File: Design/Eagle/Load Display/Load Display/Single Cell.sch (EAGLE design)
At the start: 1 part

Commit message: Added some eagle files
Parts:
- added 12VPOWER, 3.3VPOWER, I2C: M025MM, Ben-SF-Con:M025MM
- added R1, R2, R3, R4, R5, R6, R7: 200, Ben-rcl:R-US_0207/10
- added U$3: HT16K33BRD, Parts:HT16K33BRD
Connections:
- new net N$1: DIS1.A, R1.2
- new net N$10: R3.1, U$3.C2
- new net N$11: R4.1, U$3.C3
- new net N$12: R5.1, U$3.C4
- new net N$13: R6.1, U$3.C5
- new net N$14: R7.1, U$3.C6
- new net N$15: I2C.1, U$3.SDA
- new net N$16: I2C.2, U$3.SCL
- new net N$17: 12VPOWER.1, 3.3VPOWER.1, U$3.GND
- new net N$18: DIS1.DP, U$3.C7
- new net N$19: 3.3VPOWER.2, U$3.VDD
- new net N$2: DIS1.B, R2.2
- new net N$20: 12VPOWER.2, DIS1.CA, DIS1.CA@1
- new net N$3: DIS1.C, R3.2
- new net N$4: DIS1.D, R4.2
- new net N$5: DIS1.E, R5.2
- new net N$6: DIS1.F, R6.2
- new net N$7: DIS1.G, R7.2
- new net N$8: R1.1, U$3.C0
- new net N$9: R2.1, U$3.C1
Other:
- moved on the sheet: DIS1

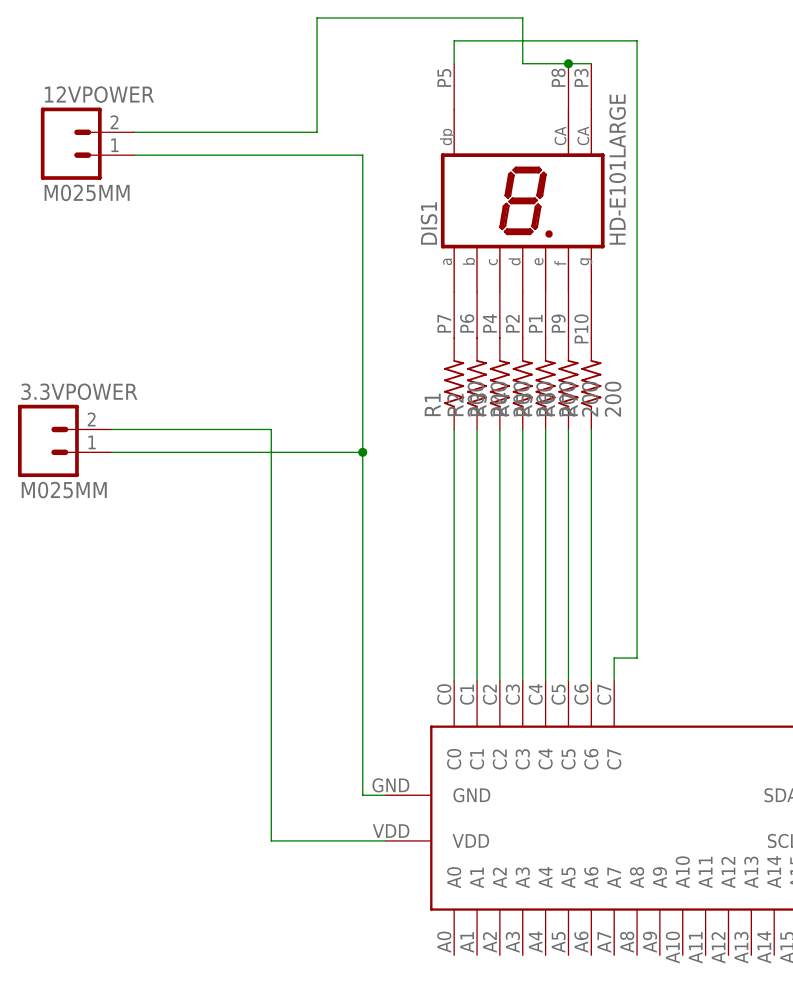
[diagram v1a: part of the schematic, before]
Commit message: Added a 5V regulator
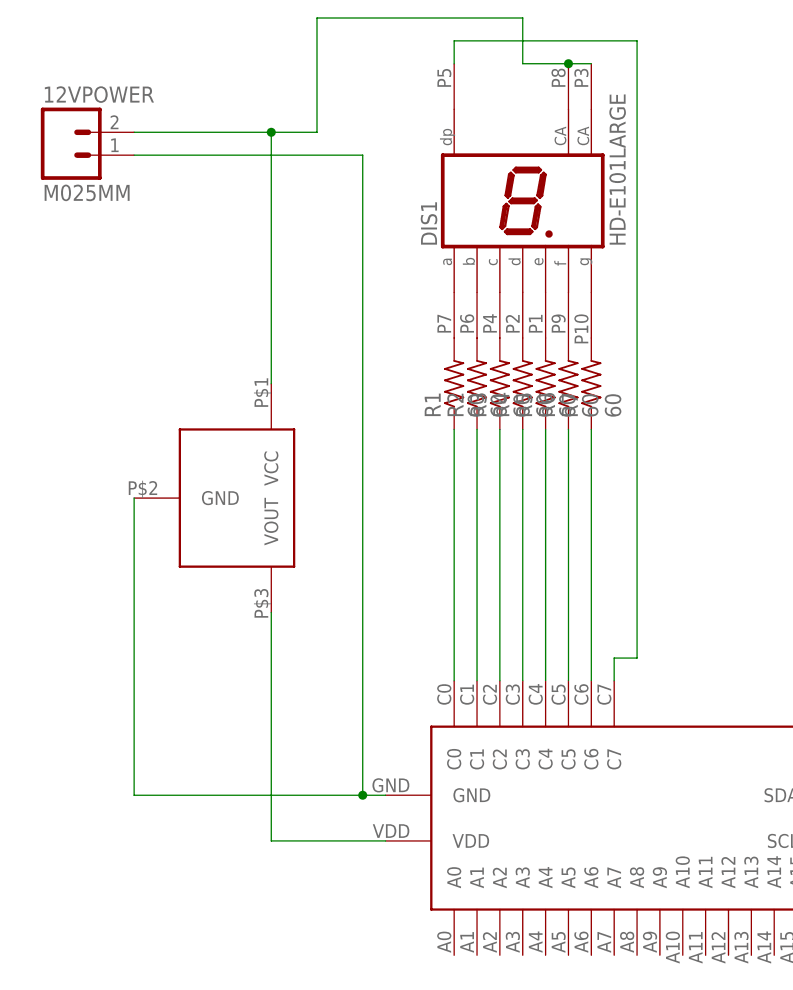
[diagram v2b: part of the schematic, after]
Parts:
- removed 3.3VPOWER: M025MM, Ben-SF-Con:M025MM
- added U$1: 5VREG, Parts:5VREG
- R1, R2, R3, R4, R5, R6, R7: value 200 -> 60
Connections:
- net N$17: now also U$1.GND; no longer 3.3VPOWER.1
- net N$19: now also U$1.VOUT; no longer 3.3VPOWER.2
- net N$20: now also U$1.VCC
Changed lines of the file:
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@@
 <part name="DIS1" library="Parts" deviceset="HD-E101" device="LARGE"/>
 <part name="U$3" library="Parts" deviceset="HT16K33BRD" device=""/>
-<part name="R1" library="Ben-rcl" deviceset="R-US_" device="0207/10" value="200"/>
-<part name="R2" library="Ben-rcl" deviceset="R-US_" device="0207/10" value="200"/>
-<part name="R3" library="Ben-rcl" deviceset="R-US_" device="0207/10" value="200"/>
-<part name="R4" library="Ben-rcl" deviceset="R-US_" device="0207/10" value="200"/>
-<part name="R5" library="Ben-rcl" deviceset="R-US_" device="0207/10" value="200"/>
-<part name="R6" library="Ben-rcl" deviceset="R-US_" device="0207/10" value="200"/>
-<part name="R7" library="Ben-rcl" deviceset="R-US_" device="0207/10" value="200"/>
+<part name="R1" library="Ben-rcl" deviceset="R-US_" device="0207/10" value="60"/>
+<part name="R2" library="Ben-rcl" deviceset="R-US_" device="0207/10" value="60"/>
+<part name="R3" library="Ben-rcl" deviceset="R-US_" device="0207/10" value="60"/>
+<part name="R4" library="Ben-rcl" deviceset="R-US_" device="0207/10" value="60"/>
+<part name="R5" library="Ben-rcl" deviceset="R-US_" device="0207/10" value="60"/>
+<part name="R6" library="Ben-rcl" deviceset="R-US_" device="0207/10" value="60"/>
+<part name="R7" library="Ben-rcl" deviceset="R-US_" device="0207/10" value="60"/>
 <part name="12VPOWER" library="Ben-SF-Con" deviceset="M02" device="5MM"/>
 <part name="I2C" library="Ben-SF-Con" deviceset="M02" device="5MM"/>
-<part name="3.3VPOWER" library="Ben-SF-Con" deviceset="M02" device="5MM"/>
+<part name="U$1" library="Parts" deviceset="5VREG" device=""/>
 </parts>
 <sheets>
@@
 <instance part="12VPOWER" gate="G$1" x="15.24" y="93.98"/>
 <instance part="I2C" gate="G$1" x="129.54" y="20.32" rot="R180"/>
-<instance part="3.3VPOWER" gate="G$1" x="12.7" y="60.96"/>
+<instance part="U$1" gate="G$1" x="38.1" y="55.88" rot="R270"/>
 </instances>
 <busses>
@@
 <pinref part="U$3" gate="G$1" pin="GND"/>
 <wire x1="50.8" y1="22.86" x2="48.26" y2="22.86" width="0.1524" layer="91"/>
-<wire x1="48.26" y1="22.86" x2="48.26" y2="60.96" width="0.1524" layer="91"/>
-<pinref part="3.3VPOWER" gate="G$1" pin="1"/>
-<wire x1="48.26" y1="60.96" x2="20.32" y2="60.96" width="0.1524" layer="91"/>
-<wire x1="48.26" y1="60.96" x2="48.26" y2="93.98" width="0.1524" layer="91"/>
-<junction x="48.26" y="60.96"/>
+<wire x1="48.26" y1="22.86" x2="48.26" y2="93.98" width="0.1524" layer="91"/>
 <pinref part="12VPOWER" gate="G$1" pin="1"/>
 <wire x1="48.26" y1="93.98" x2="22.86" y2="93.98" width="0.1524" layer="91"/>
+<pinref part="U$1" gate="G$1" pin="GND"/>
+<wire x1="48.26" y1="22.86" x2="22.86" y2="22.86" width="0.1524" layer="91"/>
+<wire x1="22.86" y1="22.86" x2="22.86" y2="55.88" width="0.1524" layer="91"/>
+<junction x="48.26" y="22.86"/>
 </segment>
 </net>
@@
 <pinref part="U$3" gate="G$1" pin="VDD"/>
 <wire x1="50.8" y1="17.78" x2="38.1" y2="17.78" width="0.1524" layer="91"/>
-<wire x1="38.1" y1="17.78" x2="38.1" y2="63.5" width="0.1524" layer="91"/>
-<pinref part="3.3VPOWER" gate="G$1" pin="2"/>
-<wire x1="38.1" y1="63.5" x2="20.32" y2="63.5" width="0.1524" layer="91"/>
+<pinref part="U$1" gate="G$1" pin="VOUT"/>
+<wire x1="38.1" y1="43.18" x2="38.1" y2="17.78" width="0.1524" layer="91"/>
 </segment>
 </net>
@@
 <wire x1="43.18" y1="109.22" x2="43.18" y2="96.52" width="0.1524" layer="91"/>
 <pinref part="12VPOWER" gate="G$1" pin="2"/>
-<wire x1="43.18" y1="96.52" x2="22.86" y2="96.52" width="0.1524" layer="91"/>
+<wire x1="43.18" y1="96.52" x2="38.1" y2="96.52" width="0.1524" layer="91"/>
+<pinref part="U$1" gate="G$1" pin="VCC"/>
+<wire x1="38.1" y1="96.52" x2="22.86" y2="96.52" width="0.1524" layer="91"/>
+<wire x1="38.1" y1="68.58" x2="38.1" y2="96.52" width="0.1524" layer="91"/>
+<junction x="38.1" y="96.52"/>
 </segment>
 </net>

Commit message: Added a lot of eagle stuff
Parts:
- DIS1: value HD-E101LARGE -> HD-E101BIG; device Parts:HD-E101LARGE -> Parts:HD-E101BIG
- R6, R7: device Ben-rcl:R-US_0207/10 -> Ben-rcl:R-US_0207/15
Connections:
- net N$20: no longer DIS1.CA
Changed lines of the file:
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@@
 <?xml version="1.0" encoding="utf-8"?>
 <!DOCTYPE eagle SYSTEM "eagle.dtd">
-<eagle version="6.2">
+<eagle version="6.5.0">
 <drawing>
 <settings>
@@
 <grid distance="0.1" unitdist="inch" unit="inch" style="lines" multiple="1" display="no" altdistance="0.01" altunitdist="inch" altunit="inch"/>
 <layers>
-<layer number="1" name="Top" color="4" fill="1" visible="no" active="no"/>
-<layer number="16" name="Bottom" color="1" fill="1" visible="no" active="no"/>
-<layer number="17" name="Pads" color="2" fill="1" visible="no" active="no"/>
-<layer number="18" name="Vias" color="2" fill="1" visible="no" active="no"/>
-<layer number="19" name="Unrouted" color="6" fill="1" visible="no" active="no"/>
-<layer number="20" name="Dimension" color="15" fill="1" visible="no" active="no"/>
-<layer number="21" name="tPlace" color="7" fill="1" visible="no" active="no"/>
-<layer number="22" name="bPlace" color="7" fill="1" visible="no" active="no"/>
-<layer number="23" name="tOrigins" color="15" fill="1" visible="no" active="no"/>
-<layer number="24" name="bOrigins" color="15" fill="1" visible="no" active="no"/>
-<layer number="25" name="tNames" color="7" fill="1" visible="no" active="no"/>
-<layer number="26" name="bNames" color="7" fill="1" visible="no" active="no"/>
-<layer number="27" name="tValues" color="7" fill="1" visible="no" active="no"/>
-<layer number="28" name="bValues" color="7" fill="1" visible="no" active="no"/>
+<layer number="1" name="Top" color="4" fill="1" visible="yes" active="no"/>
+<layer number="16" name="Bottom" color="1" fill="1" visible="yes" active="no"/>
+<layer number="17" name="Pads" color="2" fill="1" visible="yes" active="no"/>
+<layer number="18" name="Vias" color="2" fill="1" visible="yes" active="no"/>
+<layer number="19" name="Unrouted" color="6" fill="1" visible="yes" active="no"/>
+<layer number="20" name="Dimension" color="15" fill="1" visible="yes" active="no"/>
+<layer number="21" name="tPlace" color="7" fill="1" visible="yes" active="no"/>
+<layer number="22" name="bPlace" color="7" fill="1" visible="yes" active="no"/>
+<layer number="23" name="tOrigins" color="15" fill="1" visible="yes" active="no"/>
+<layer number="24" name="bOrigins" color="15" fill="1" visible="yes" active="no"/>
+<layer number="25" name="tNames" color="7" fill="1" visible="yes" active="no"/>
+<layer number="26" name="bNames" color="7" fill="1" visible="yes" active="no"/>
+<layer number="27" name="tValues" color="7" fill="1" visible="yes" active="no"/>
+<layer number="28" name="bValues" color="7" fill="1" visible="yes" active="no"/>
 <layer number="29" name="tStop" color="7" fill="3" visible="no" active="no"/>
 <layer number="30" name="bStop" color="7" fill="6" visible="no" active="no"/>
@@
 <layer number="35" name="tGlue" color="7" fill="4" visible="no" active="no"/>
 <layer number="36" name="bGlue" color="7" fill="5" visible="no" active="no"/>
-<layer number="37" name="tTest" color="7" fill="1" visible="no" active="no"/>
-<layer number="38" name="bTest" color="7" fill="1" visible="no" active="no"/>
+<layer number="37" name="tTest" color="7" fill="1" visible="yes" active="no"/>
+<layer number="38" name="bTest" color="7" fill="1" visible="yes" active="no"/>
 <layer number="39" name="tKeepout" color="4" fill="11" visible="no" active="no"/>
 <layer number="40" name="bKeepout" color="1" fill="11" visible="no" active="no"/>
@@
 <layer number="44" name="Drills" color="7" fill="1" visible="no" active="no"/>
 <layer number="45" name="Holes" color="7" fill="1" visible="no" active="no"/>
-<layer number="46" name="Milling" color="3" fill="1" visible="no" active="no"/>
-<layer number="47" name="Measures" color="7" fill="1" visible="no" active="no"/>
-<layer number="48" name="Document" color="7" fill="1" visible="no" active="no"/>
-<layer number="49" name="Reference" color="7" fill="1" visible="no" active="no"/>
-<layer number="50" name="dxf" color="7" fill="1" visible="no" active="no"/>
-<layer number="51" name="tDocu" color="7" fill="1" visible="no" active="no"/>
-<layer number="52" name="bDocu" color="7" fill="1" visible="no" active="no"/>
-<layer number="53" name="tGND_GNDA" color="7" fill="9" visible="no" active="no"/>
-<layer number="54" name="bGND_GNDA" color="1" fill="9" visible="no" active="no"/>
-<layer number="56" name="wert" color="7" fill="1" visible="no" active="no"/>
+<layer number="46" name="Milling" color="3" fill="1" visible="yes" active="no"/>
+<layer number="47" name="Measures" color="7" fill="1" visible="yes" active="no"/>
+<layer number="48" name="Document" color="7" fill="1" visible="yes" active="no"/>
+<layer number="49" name="Reference" color="7" fill="1" visible="yes" active="no"/>
+<layer number="50" name="dxf" color="7" fill="1" visible="yes" active="no"/>
+<layer number="51" name="tDocu" color="7" fill="1" visible="yes" active="no"/>
+<layer number="52" name="bDocu" color="7" fill="1" visible="yes" active="no"/>
+<layer number="53" name="tGND_GNDA" color="7" fill="9" visible="yes" active="no"/>
+<layer number="54" name="bGND_GNDA" color="1" fill="9" visible="yes" active="no"/>
+<layer number="56" name="wert" color="7" fill="1" visible="yes" active="no"/>
 <layer number="91" name="Nets" color="2" fill="1" visible="yes" active="yes"/>
 <layer number="92" name="Busses" color="1" fill="1" visible="yes" active="yes"/>
@@
 </classes>
 <parts>
-<part name="DIS1" library="Parts" deviceset="HD-E101" device="LARGE"/>
+<part name="DIS1" library="Parts" deviceset="HD-E101" device="BIG" value="HD-E101BIG"/>
 <part name="U$3" library="Parts" deviceset="HT16K33BRD" device=""/>
 <part name="R1" library="Ben-rcl" deviceset="R-US_" device="0207/10" value="60"/>
@@
 <part name="R4" library="Ben-rcl" deviceset="R-US_" device="0207/10" value="60"/>
 <part name="R5" library="Ben-rcl" deviceset="R-US_" device="0207/10" value="60"/>
-<part name="R6" library="Ben-rcl" deviceset="R-US_" device="0207/10" value="60"/>
-<part name="R7" library="Ben-rcl" deviceset="R-US_" device="0207/10" value="60"/>
+<part name="R6" library="Ben-rcl" deviceset="R-US_" device="0207/15" value="60"/>
+<part name="R7" library="Ben-rcl" deviceset="R-US_" device="0207/15" value="60"/>
 <part name="12VPOWER" library="Ben-SF-Con" deviceset="M02" device="5MM"/>
 <part name="I2C" library="Ben-SF-Con" deviceset="M02" device="5MM"/>
@@
 <segment>
 <pinref part="DIS1" gate="A" pin="CA@1"/>
-<pinref part="DIS1" gate="A" pin="CA"/>
-<wire x1="71.12" y1="104.14" x2="73.66" y2="104.14" width="0.1524" layer="91"/>
 <wire x1="71.12" y1="104.14" x2="66.04" y2="104.14" width="0.1524" layer="91"/>
-<junction x="71.12" y="104.14"/>
 <wire x1="66.04" y1="104.14" x2="66.04" y2="109.22" width="0.1524" layer="91"/>
 <wire x1="66.04" y1="109.22" x2="43.18" y2="109.22" width="0.1524" layer="91"/>
